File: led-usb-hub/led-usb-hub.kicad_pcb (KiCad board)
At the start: 4 copper layers, 58.4 x 41.1 mm, 128 parts, among them J1 USBC_USB2.0, J2 RGBUSB_54-00266, J3 RGBUSB_54-00266, J4 RGBUSB_54-00266, J5 SWD, SW1 RESET, SW2 BOOT, SW3 LED EN, U1 STM32L552CETx, U12 MAX809, U2 TUSB2046IBVF, U3 TLV62569PDDCR, U4 TLV62569PDDCR, U5 TPS2042D, U6 TPS2042D, Y1 KC2520Z8.00000C1KX00, Y2 KC2520Z6.00000C1GX00

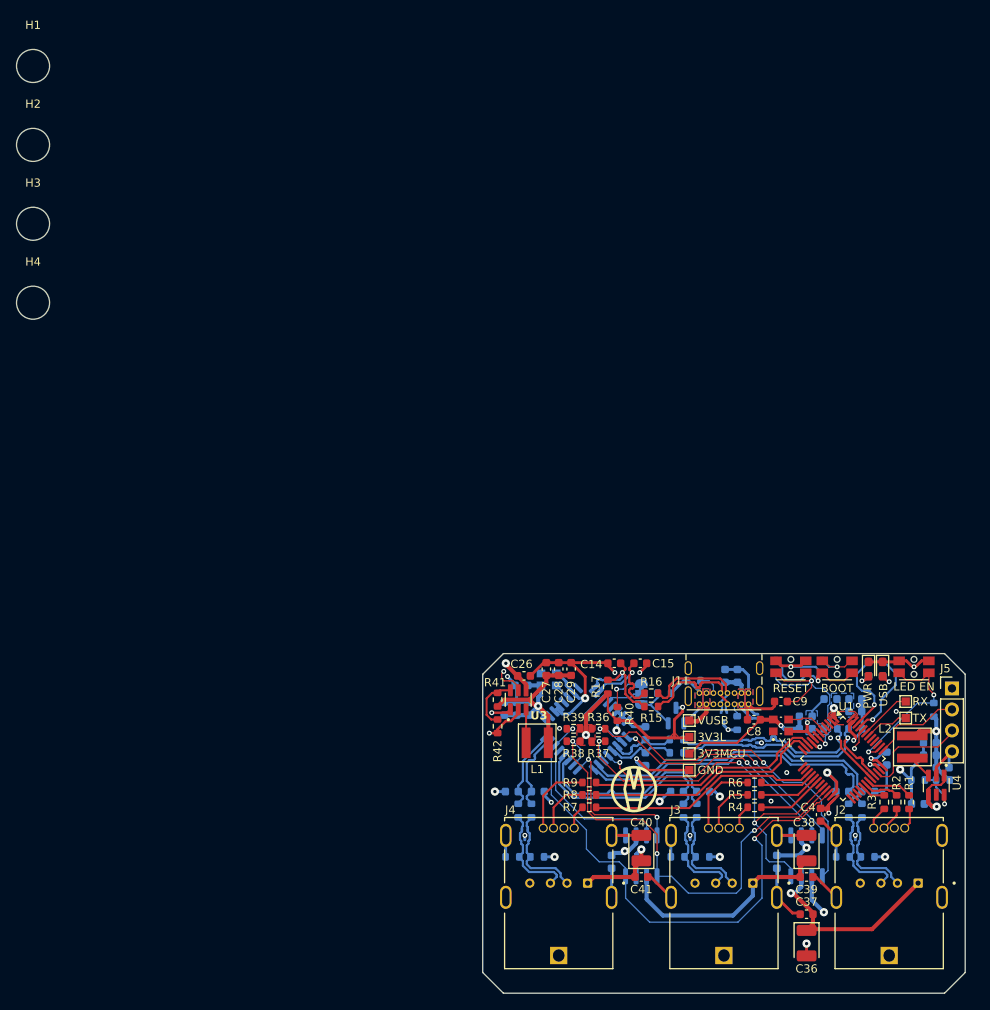
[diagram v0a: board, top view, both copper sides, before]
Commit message: [HW] Trace Clean up
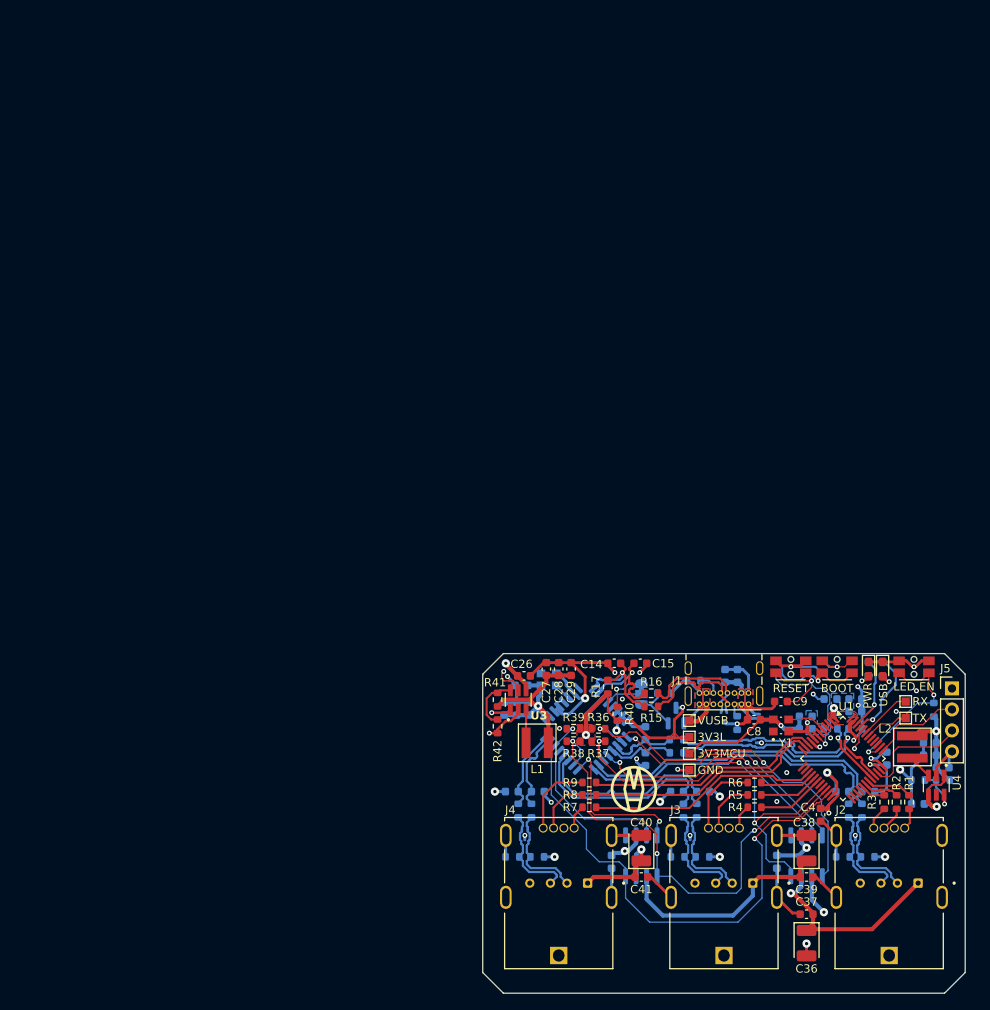
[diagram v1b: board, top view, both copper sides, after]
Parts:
- removed H1, H2, H3, H4: MountingHole, MountingHole:MountingHole_4mm
- moved D3 0.20 mm to (92.2, 83.0)
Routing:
- net Earth: track 192.4 -> 189.1 mm, vias 33 -> 38
- net LED_PWR: track 10.3 -> 8.77 mm

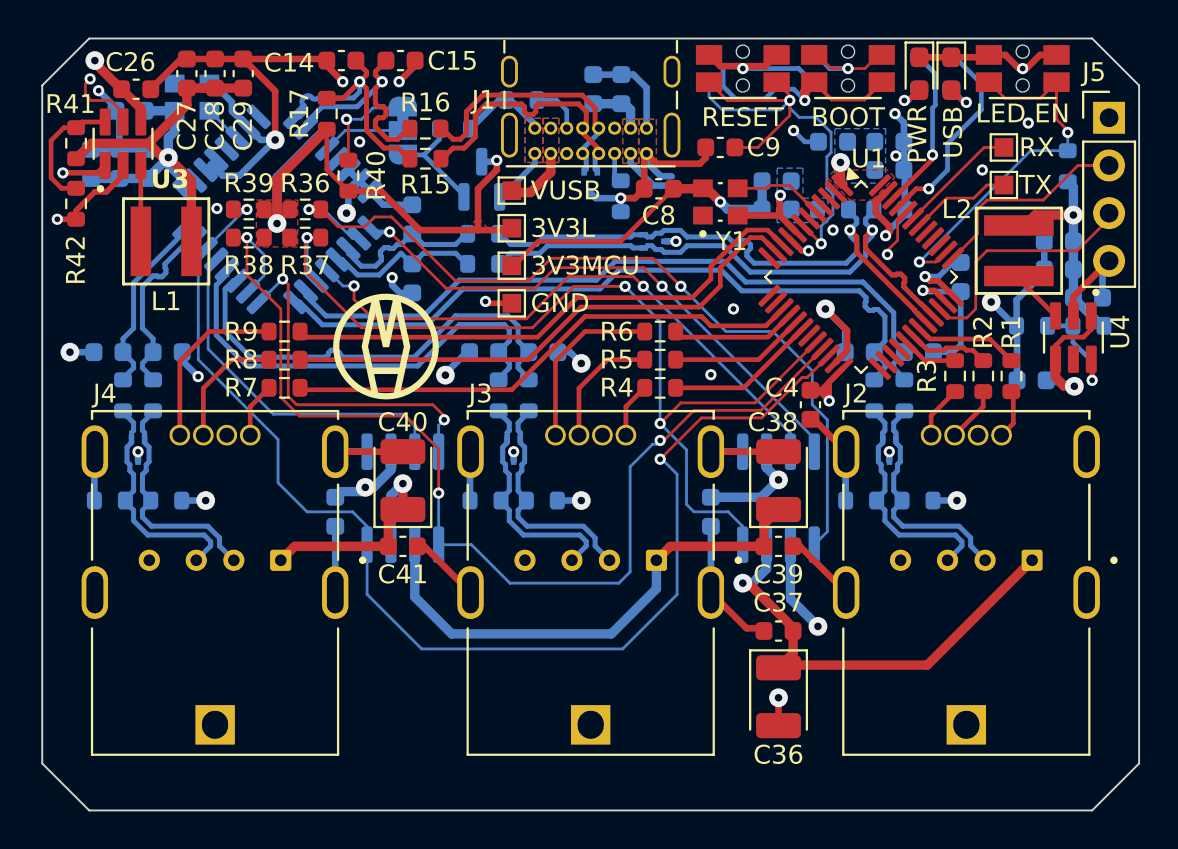
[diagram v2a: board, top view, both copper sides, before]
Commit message: [HW] Rearrange to allow port hangover board edge (better for case) TODO: Figure out mounting/alignment 	Case might provide all mounting and just need registration 	So could add semi-circles on board edge (or partial circles) to force alignment
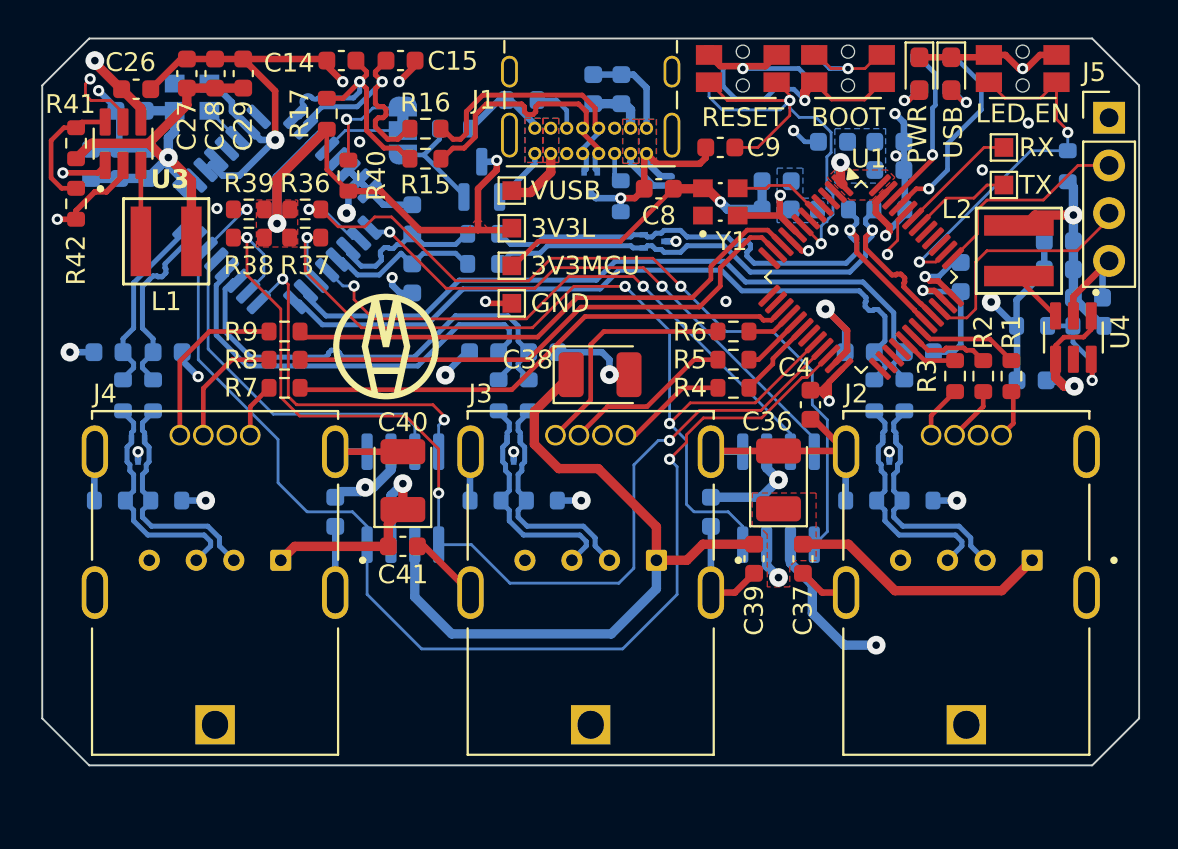
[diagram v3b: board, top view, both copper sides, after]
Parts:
- moved G3 25.9 mm to (67.9, 106.9)
- moved C36 11.5 mm to (97.9, 98.9), turned to 90 degrees
- moved C38 11.0 mm to (88.4, 93.3), turned to 0 degrees
- moved G*** 10.7 mm to (87.9, 108.8)
- moved G2 6.82 mm to (107.9, 107.2)
- moved C37 4.06 mm to (99.2, 103.1), turned to -90 degrees
- moved R4 3.90 mm to (95.5, 94.0)
- moved R5 3.90 mm to (95.5, 92.5)
- moved R6 3.90 mm to (95.5, 91.0)
- moved C39 1.46 mm to (96.6, 103.1), turned to -90 degrees
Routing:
- net +5V_2: track 27.3 -> 39.1 mm
- net +5V_1: track 24.5 -> 15.9 mm
- net L2_B: track 6.64 -> 2.50 mm
- net L2_G: track 7.22 -> 3.32 mm
- net L2_R: track 8.05 -> 4.32 mm
- net Earth: track 189.1 -> 192.6 mm, vias 38 -> 36
- net /L2_B': track 9.35 -> 12.7 mm
- net /L2_R': track 2.93 -> 5.94 mm
- net /L2_G': track 6.63 -> 9.07 mm
- net OC3: track 64.8 -> 64.2 mm
- net OC1: track 51.8 -> 51.3 mm
- added copper zone on F.Cu, net +5V_1
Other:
- board size 58.4 x 41.1 mm -> 58.4 x 38.7 mm
- board text added: "Designed by Matthew Haahr 2025"
- board text added: "RGB LED USB 2.0 Hub Rev 3"
- board text removed: "RGB LED USB 2.0 Hub Designed by Matthew Haahr - 2025"

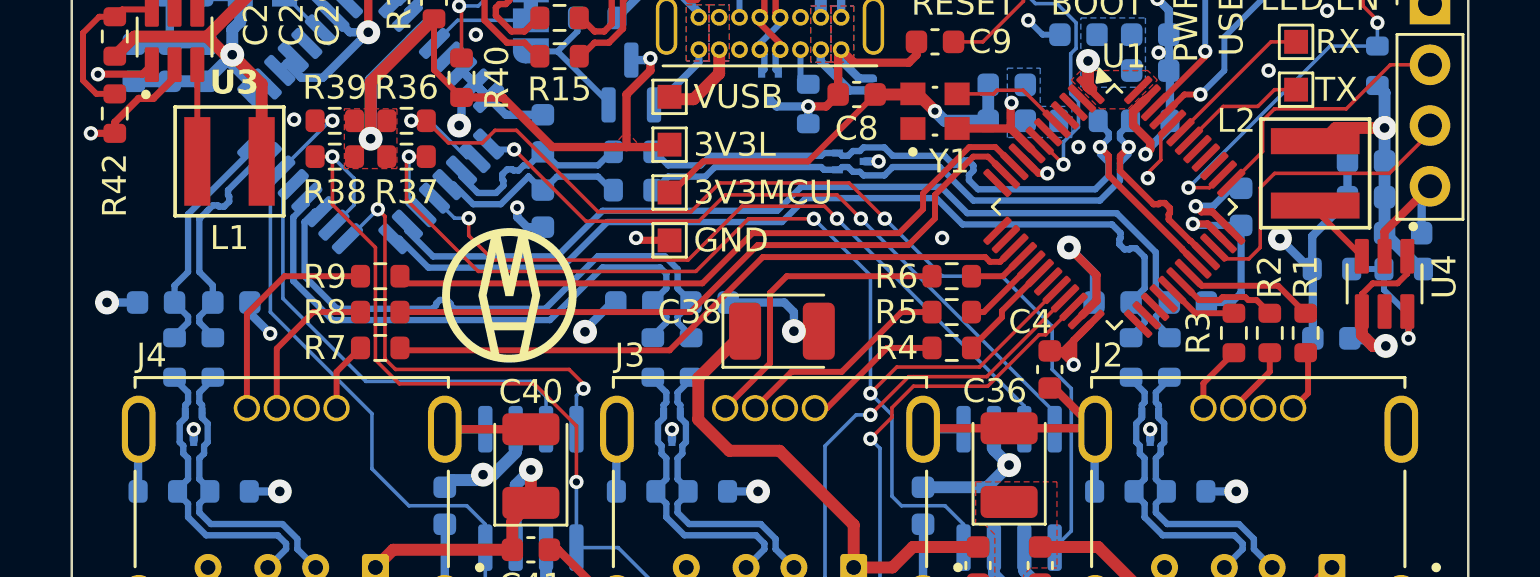
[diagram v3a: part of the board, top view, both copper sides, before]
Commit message: [HW] Add mounting/registration points, export Fab tools
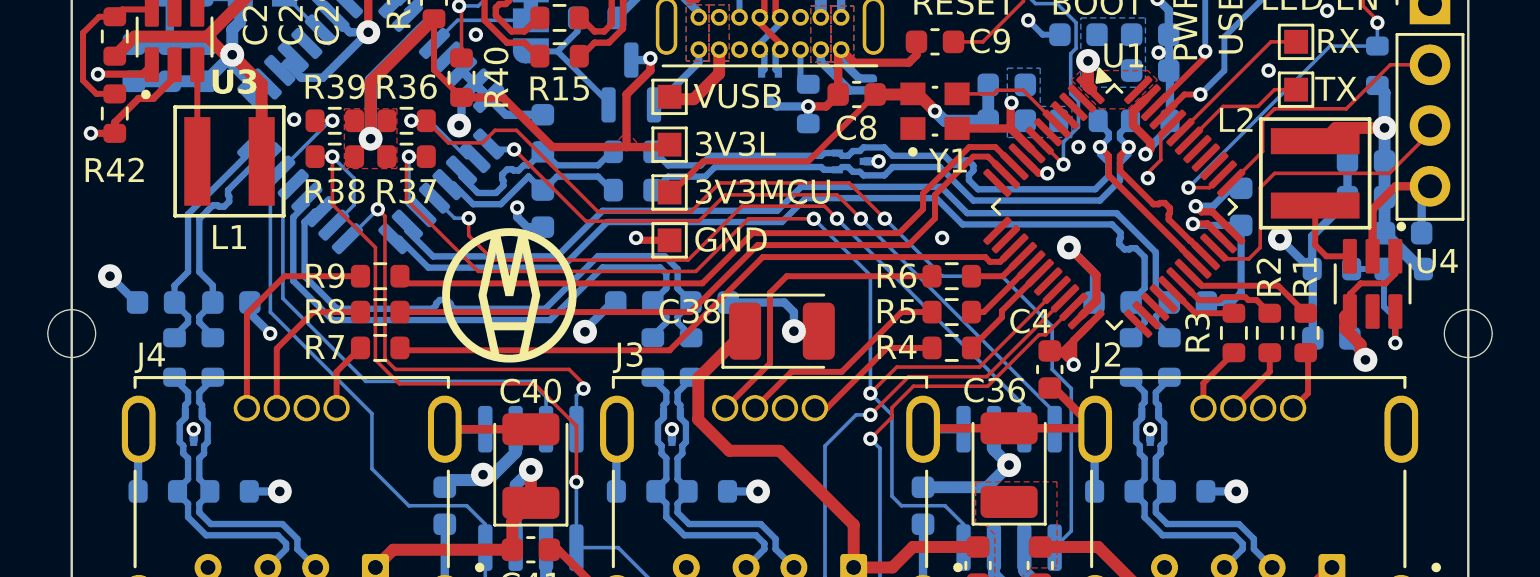
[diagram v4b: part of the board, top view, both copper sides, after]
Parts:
- added H1: MountingHole, MountingHole:MountingHole_2mm, F.Cu at (58.7, 93.4)
- added H2: MountingHole, MountingHole:MountingHole_2mm, F.Cu at (117.1, 93.4)
- moved U4 0.50 mm to (113.1, 91.3)
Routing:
- net Earth: track 192.6 -> 193.8 mm
- net +5V_0: track 37.6 -> 36.5 mm
- net /REG_MCU_SW: track 2.50 -> 3.30 mm

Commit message: [HW] More Space
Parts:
- moved C38 0.20 mm to (88.4, 93.1)
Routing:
- net Earth: track 193.8 -> 193.3 mm

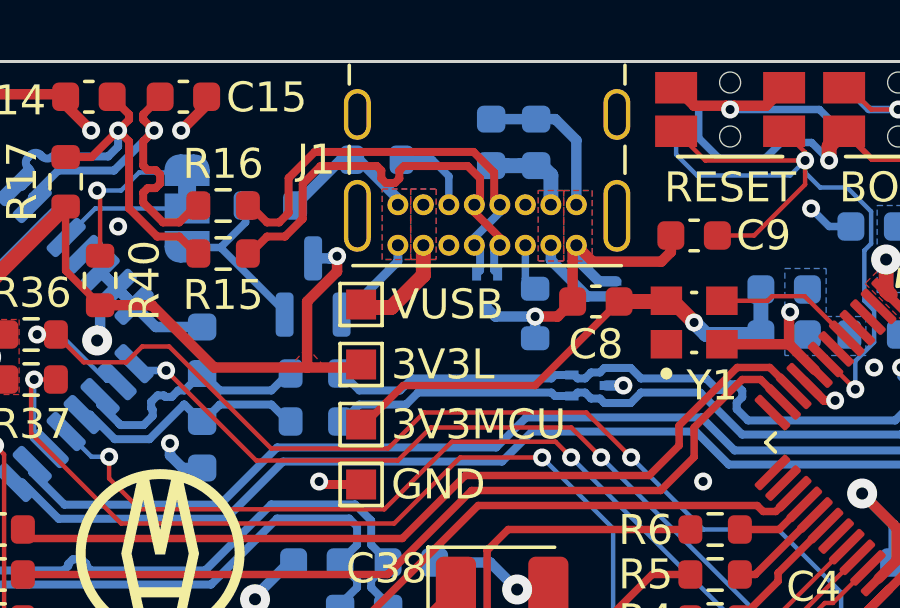
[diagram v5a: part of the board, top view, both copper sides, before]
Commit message: [HW] Update BOM and Docs
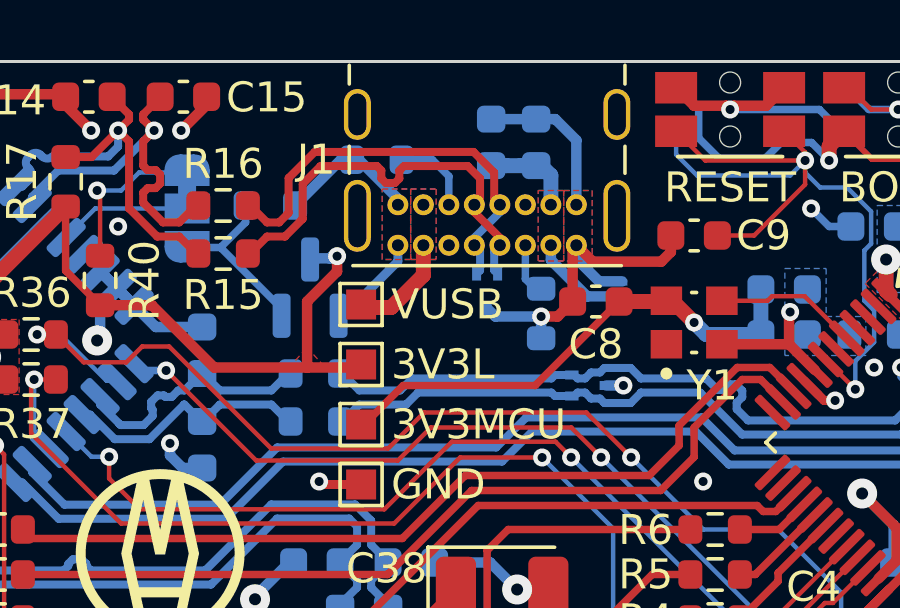
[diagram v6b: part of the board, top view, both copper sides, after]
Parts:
- removed U12: MAX809, Package_TO_SOT_SMD:SOT-23
- added U7: MAX809, Package_TO_SOT_SMD:SOT-23, B.Cu at (82.0, 82.9)
- R17: value 1k5 -> 1.5k
- R34, R35: value 5K1 -> 5.1k
- moved D3 0.20 mm to (92.4, 83.0)
- moved R35 0.20 mm to (89.7, 83.8)

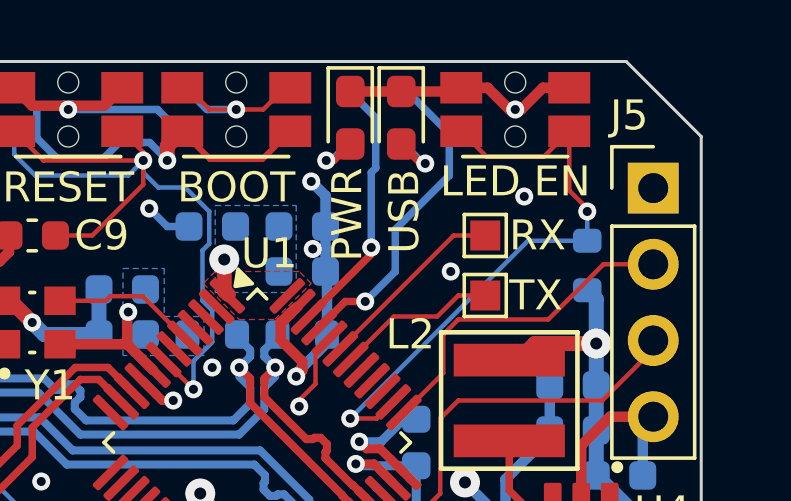
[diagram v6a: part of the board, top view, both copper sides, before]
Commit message: [HW] Switch LED to side-firing bi-color LED
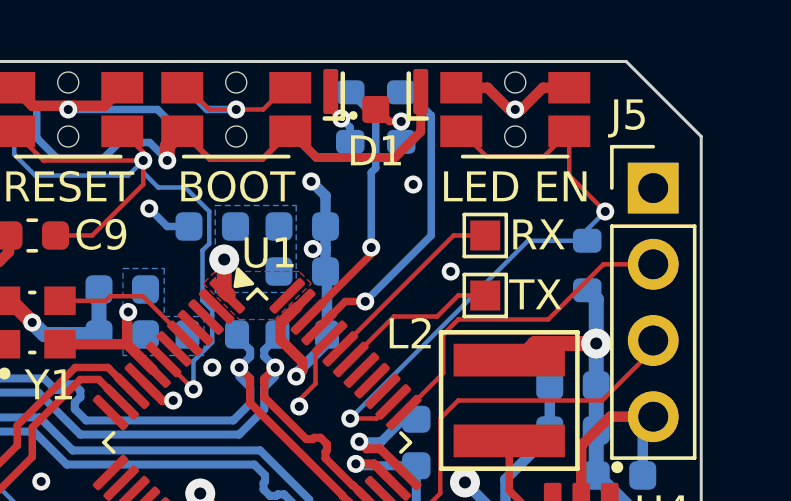
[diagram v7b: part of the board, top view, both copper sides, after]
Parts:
- removed the D2 at (107.1, 77.3)
- D1: value PWR -> ~; footprint LED_SMD:LED_0603_1608Metric_Pad1.05x0.95mm_HandSolder -> HSMF-C143:HSMF-C143
- R13: value 2k -> 1.74k
- R14: value 2.4k -> 665
- moved D1 1.79 mm to (106.2, 75.7), turned to 0 degrees
- renumbered D3 to D2, D4 to D3, D5 to D4, D6 to D5, D7 to D6, D8 to D7
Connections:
- D1 pad 1: Earth -> /LED_PWR'
- D1 pad 2: /LED_PWR' -> /LED_USB'
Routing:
- net +3V3_MCU: track 168.3 -> 174.8 mm
- net Earth: track 193.5 -> 189.9 mm
